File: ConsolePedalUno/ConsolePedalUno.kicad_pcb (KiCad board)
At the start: 2 copper layers, 100 x 60 mm, 53 parts, among them J1 Conn_02x25_Counter_Clockwise, J2 EXT, SW1 SW_Push, SW2 SW_Push, SW3 SW_Push, SW4 SW_Push, U1 TL972, U2 ATmega328P-PU, U3 LM7805_TO220, Y1 16MHz

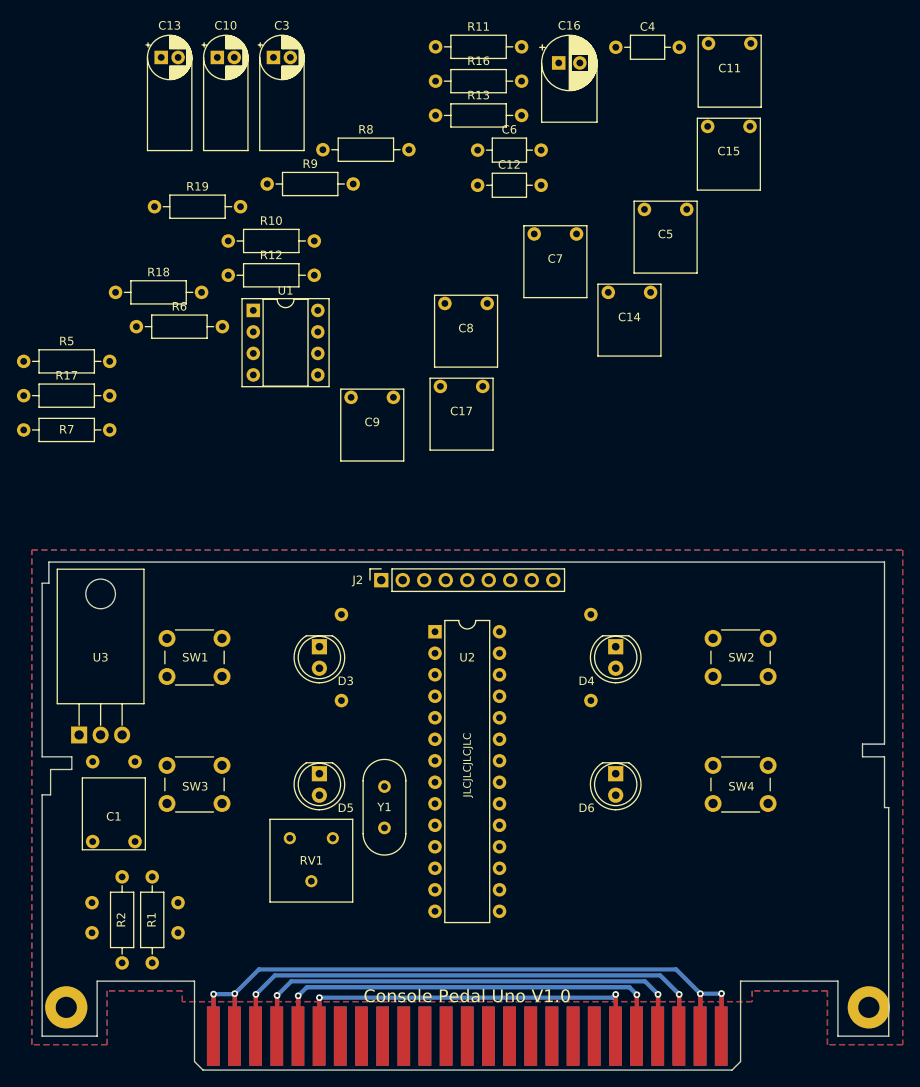
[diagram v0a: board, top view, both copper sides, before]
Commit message: Finalized and exported Uno board
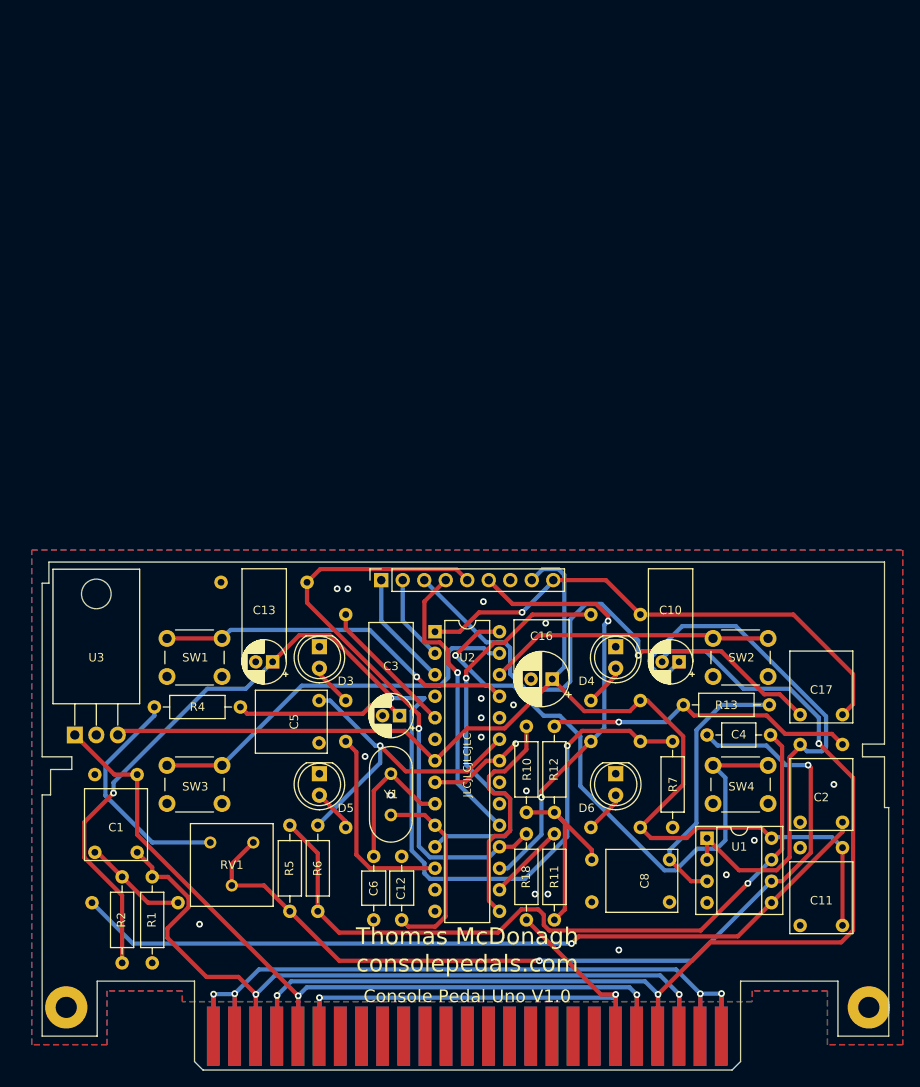
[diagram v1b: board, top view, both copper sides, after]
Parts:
- C14, C15, C7, C9, R16, R17, R19, R8, R9: moved to B.Cu
- C2, R4: moved to F.Cu
- moved C11 104.6 mm to (177.0, 112.5), turned to 180 degrees
- moved R11 104.1 mm to (143.0, 112.3), turned to 90 degrees
- moved C6 91.7 mm to (121.7, 112.3), turned to 90 degrees
- moved C10 89.8 mm to (157.7, 81.8), turned to 180 degrees
- moved R18 88.6 mm to (139.7, 112.3), turned to 90 degrees
- moved R8 88.4 mm to (153.2, 101.3), turned to 90 degrees
- moved C12 87.2 mm to (125.0, 112.3), turned to 90 degrees
- moved C15 86.7 mm to (177.0, 104.1), turned to 180 degrees
- moved R7 85.0 mm to (157.0, 91.2), turned to 270 degrees
- moved C2 83.8 mm to (177.0, 100.3)
- moved U1 82.2 mm to (161.0, 102.6)
- moved C4 81.9 mm to (161.0, 90.4)
- moved C14 79.6 mm to (93.7, 95.5), turned to 180 degrees
- moved C3 79.2 mm to (124.7, 88.1), turned to 180 degrees
- moved R16 78.7 mm to (118.4, 91.2), turned to 270 degrees
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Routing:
- net +5V: track 0.00 -> 142.0 mm
- net +2V5: track 0.00 -> 137.3 mm, vias 0 -> 3
- net Net-(C4-Pad1): track 0.00 -> 107.4 mm, vias 0 -> 2
- net Net-(C2-Pad1): track 0.00 -> 97.2 mm, vias 0 -> 1
- net Net-(C4-Pad2): track 0.00 -> 88.3 mm, vias 0 -> 1
- net /Output: track 66.0 -> 141.4 mm, vias 2 -> 3
- net /DIG_12: track 0.00 -> 71.2 mm, vias 0 -> 1
- net /A5: track 0.00 -> 69.6 mm, vias 0 -> 1
- net Net-(C10-Pad1): track 0.00 -> 67.1 mm
- net Net-(C17-Pad2): track 0.00 -> 66.9 mm, vias 0 -> 1
- net /pin1: track 0.00 -> 61.9 mm, vias 0 -> 1
- net /DIG_11: track 0.00 -> 51.5 mm, vias 0 -> 2
- net /DIG_5: track 0.00 -> 48.9 mm, vias 0 -> 1
- net /A4: track 0.00 -> 47.0 mm
- net +9V: track 60.1 -> 103.4 mm
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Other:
- board text added: "Thomas McDonagh consolepedals.com"
